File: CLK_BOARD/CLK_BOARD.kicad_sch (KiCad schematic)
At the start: 83 parts, among them J1 PWR, J2 OUT_50M_1, J3 OUT_50M_2, J4 OUT_50M_3, J5 OUT_50M_4, J6 OUT_100M_3, J7 OUT_100M_2, J8 OUT_100M_1, J9 Conn_01x04, U1 TPS7A9101DSKR, U2 LMK00804BQWRGTRQ1, U3 LMK00804BQWRGTRQ1, U4 SN74LVC1G74DCUR, X1 TB612-100.0M

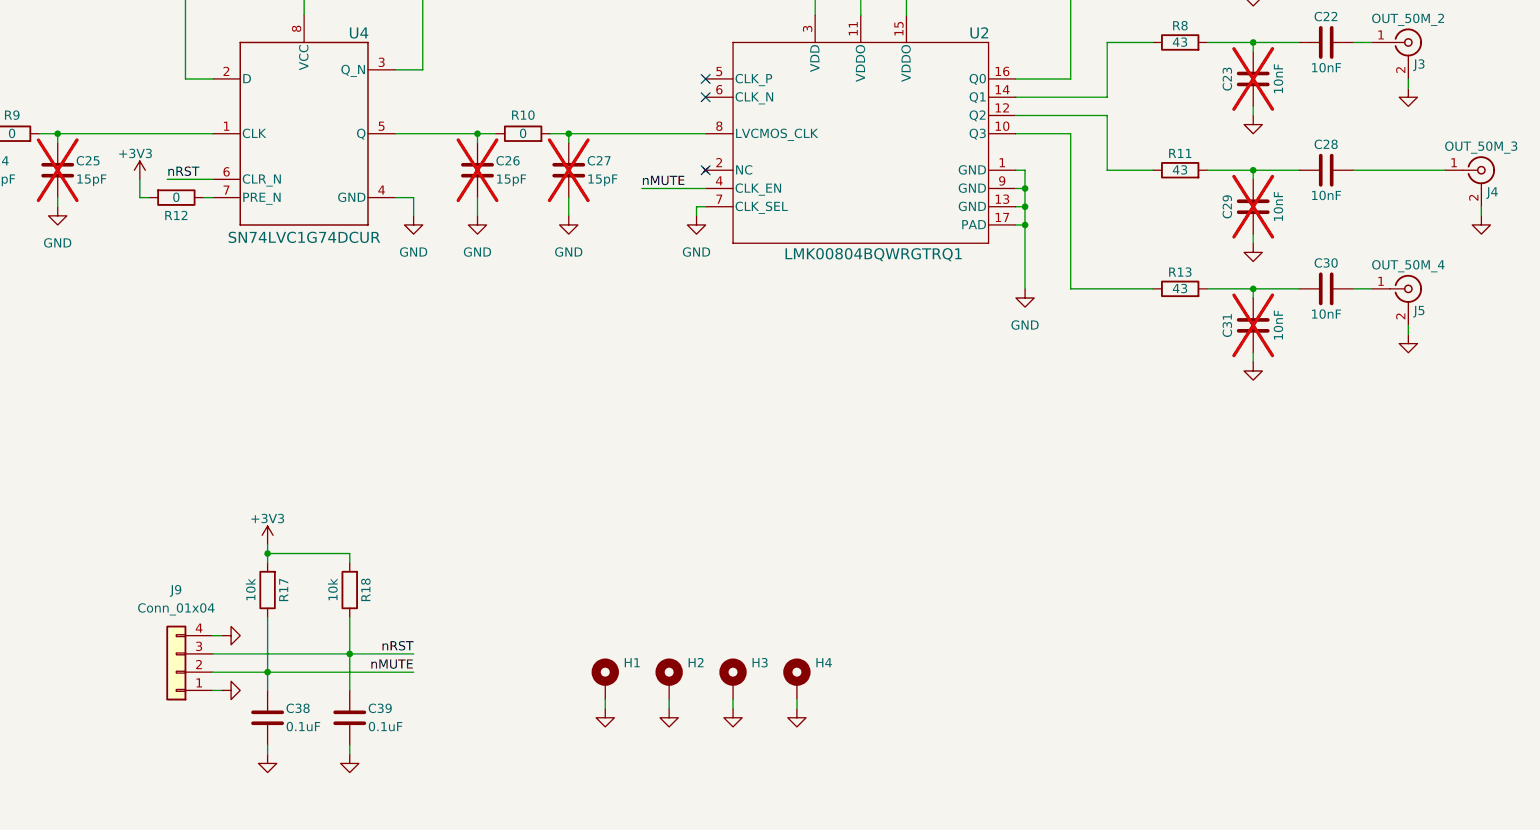
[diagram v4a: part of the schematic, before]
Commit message: redid layout with QFN package instead of TSOP
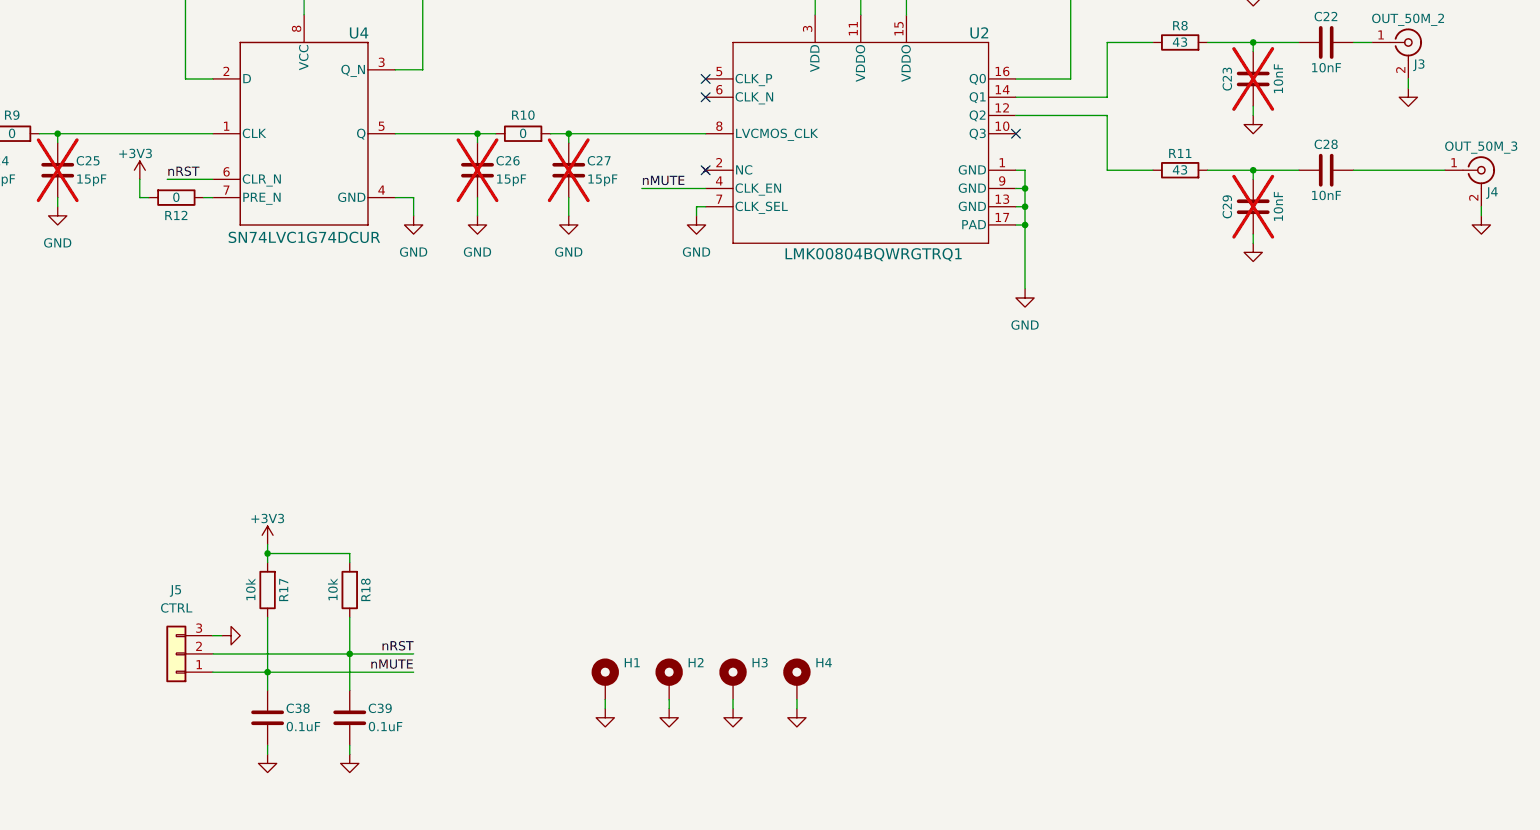
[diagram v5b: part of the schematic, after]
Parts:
- removed C30, C31: 10nF, Capacitor_SMD:C_0402_1005Metric, symbol Device:C
- removed J5: OUT_50M_4, Connector_Coaxial:SMA_Samtec_SMA-J-P-H-ST-EM1_EdgeMount, symbol Connector:Conn_Coaxial
- removed J9: Conn_01x04, Connector_PinHeader_2.54mm:PinHeader_1x04_P2.54mm_Vertical, symbol Connector_Generic:Conn_01x04
- removed R13: 43, Resistor_SMD:R_0402_1005Metric, symbol Device:R
- added J5: CTRL, Connector_PinHeader_2.54mm:PinHeader_1x03_P2.54mm_Vertical, symbol Connector_Generic:Conn_01x03
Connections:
- net GND: now also J5.3 (Pin_3)
- net nMUTE: now also J5.1 (Pin_1)
- net nRST: now also J5.2 (Pin_2)
- no-connect marks 7 -> 8

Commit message: cleanup
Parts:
- C10, C11, C14, C19, C20, C21, C38, C39, C9: Dielectric (none) -> X7R; MPN (none) -> GRM188R72A104KA35D; Manufacturer (none) -> Murata; Tolerance (none) -> +/-10%; Voltage (none) -> 25V
- C12, C17, C7: Dielectric (none) -> X5R; MPN (none) -> GRT188R61A106KE13D; Manufacturer (none) -> Murata; Tolerance (none) -> +/-10%; Voltage (none) -> 16V
- C13, C18, C8: Dielectric (none) -> X7R; MPN (none) -> 885012206052; Manufacturer (none) -> Würth Elektronik; Tolerance (none) -> +/-10%; Voltage (none) -> 25V
- C15, C16, C22, C23, C28, C29, C32, C33, C34, C35, C36, C37: Dielectric (none) -> X7R; MPN (none) -> GRM155R71H103KA88D; Manufacturer (none) -> Murata; Tolerance (none) -> +/-10%; Voltage (none) -> 50V
- C24, C25, C26, C27, C40, C41: Dielectric (none) -> C0G/NP0; MPN (none) -> GRM1555C1H150JA01D; Manufacturer (none) -> Murata; Tolerance (none) -> +/-5%; Voltage (none) -> 50V
- J2, J3, J4, J6, J7, J8: MPN (none) -> SMA-J-P-H-ST-EM1; Manufacturer (none) -> Samtec
- R10, R12, R20, R9: MPN (none) -> RC0402JR-070RL; Manufacturer (none) -> Yageo; Tolerance (none) -> +/-5%
- R11, R14, R15, R16, R6, R8: MPN (none) -> RC0402FR-0743RL; Manufacturer (none) -> Yageo; Tolerance (none) -> +/-1%
- R4, R5, R7: MPN (none) -> RC0603JR-070RL; Manufacturer (none) -> Yageo; Tolerance (none) -> +/-5%
- U1: MPN (none) -> TPS7A9101DSKR; Manufacturer (none) -> Texas Instruments
- U2, U3: MPN (none) -> LMK00804BQWRGTRQ1; Manufacturer (none) -> Texas Instruments
- U4: MPN (none) -> SN74LVC1G74DCUR; Manufacturer (none) -> Texas Instruments
- X1: MPN (none) -> TB612-100.0M; Manufacturer (none) -> Connor-Winfield

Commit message: ported footprint changes to library, will be redoing the layout from the beginning because i was not happy with the result
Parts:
- J2, J3, J4, J6, J7, J8: footprint Connector_Coaxial:SMA_Samtec_SMA-J-P-H-ST-EM1_EdgeMount -> Snapeda:SMA_Samtec_SMA-J-P-H-ST-EM1_EdgeMount
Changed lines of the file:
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@@
 			)
 		)
-		(property "Footprint" "Connector_Coaxial:SMA_Samtec_SMA-J-P-H-ST-EM1_EdgeMount"
+		(property "Footprint" "Snapeda:SMA_Samtec_SMA-J-P-H-ST-EM1_EdgeMount"
 			(at 138.43 194.31 0)
 			(hide yes)
@@
 			)
 		)
-		(property "Footprint" "Connector_Coaxial:SMA_Samtec_SMA-J-P-H-ST-EM1_EdgeMount"
+		(property "Footprint" "Snapeda:SMA_Samtec_SMA-J-P-H-ST-EM1_EdgeMount"
 			(at 384.81 125.73 0)
 			(hide yes)
@@
 			)
 		)
-		(property "Footprint" "Connector_Coaxial:SMA_Samtec_SMA-J-P-H-ST-EM1_EdgeMount"
+		(property "Footprint" "Snapeda:SMA_Samtec_SMA-J-P-H-ST-EM1_EdgeMount"
 			(at 157.48 194.31 0)
 			(hide yes)
@@
 			)
 		)
-		(property "Footprint" "Connector_Coaxial:SMA_Samtec_SMA-J-P-H-ST-EM1_EdgeMount"
+		(property "Footprint" "Snapeda:SMA_Samtec_SMA-J-P-H-ST-EM1_EdgeMount"
 			(at 175.26 194.31 0)
 			(hide yes)
@@
 			)
 		)
-		(property "Footprint" "Connector_Coaxial:SMA_Samtec_SMA-J-P-H-ST-EM1_EdgeMount"
+		(property "Footprint" "Snapeda:SMA_Samtec_SMA-J-P-H-ST-EM1_EdgeMount"
 			(at 394.97 143.51 0)
 			(hide yes)
@@
 			)
 		)
-		(property "Footprint" "Connector_Coaxial:SMA_Samtec_SMA-J-P-H-ST-EM1_EdgeMount"
+		(property "Footprint" "Snapeda:SMA_Samtec_SMA-J-P-H-ST-EM1_EdgeMount"
 			(at 394.97 107.95 0)
 			(hide yes)

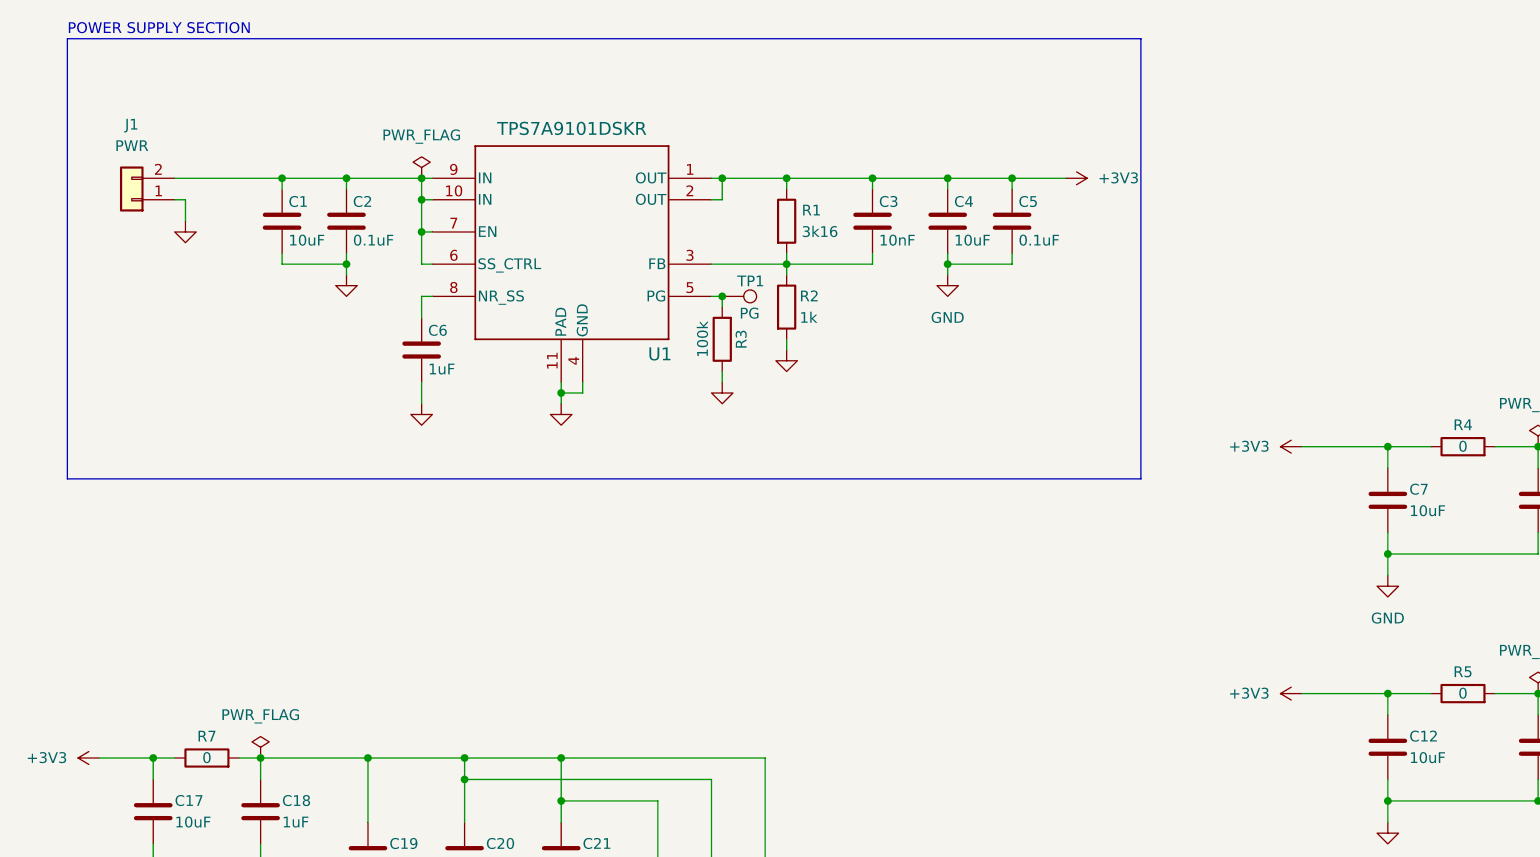
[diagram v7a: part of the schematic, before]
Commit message: fixed some real issues, no DRC errors now
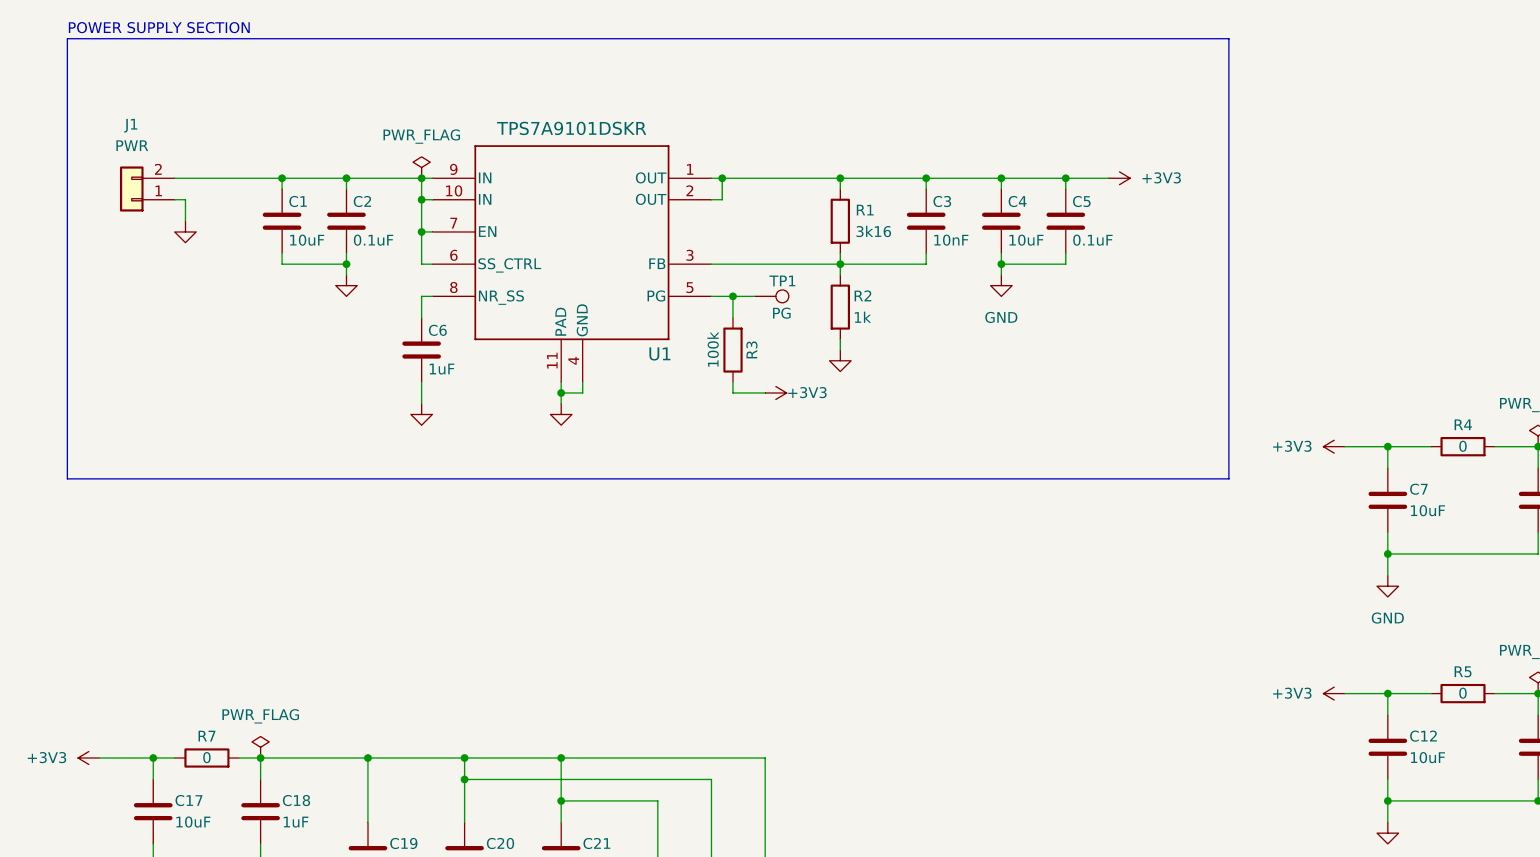
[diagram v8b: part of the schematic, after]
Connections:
- net +3V3: now also R3.1
- net GND: no longer R3.1
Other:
- moved on the sheet: C3, C4, C5, R1, R2, R3, TP1
